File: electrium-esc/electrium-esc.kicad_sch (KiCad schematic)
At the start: 31 parts, among them J2 USB_MICRO, J4 SERVO, J5 Conn_01x04_Male

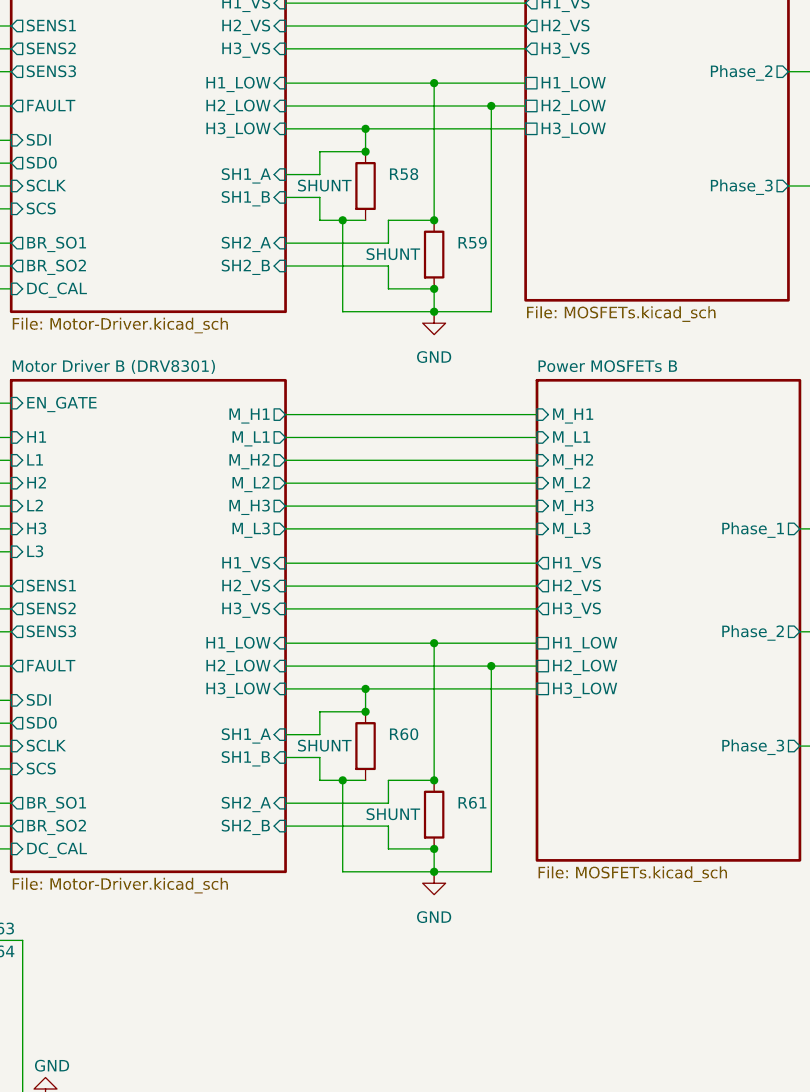
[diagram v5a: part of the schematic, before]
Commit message: Add Shunt resistors and fixed DRC errors
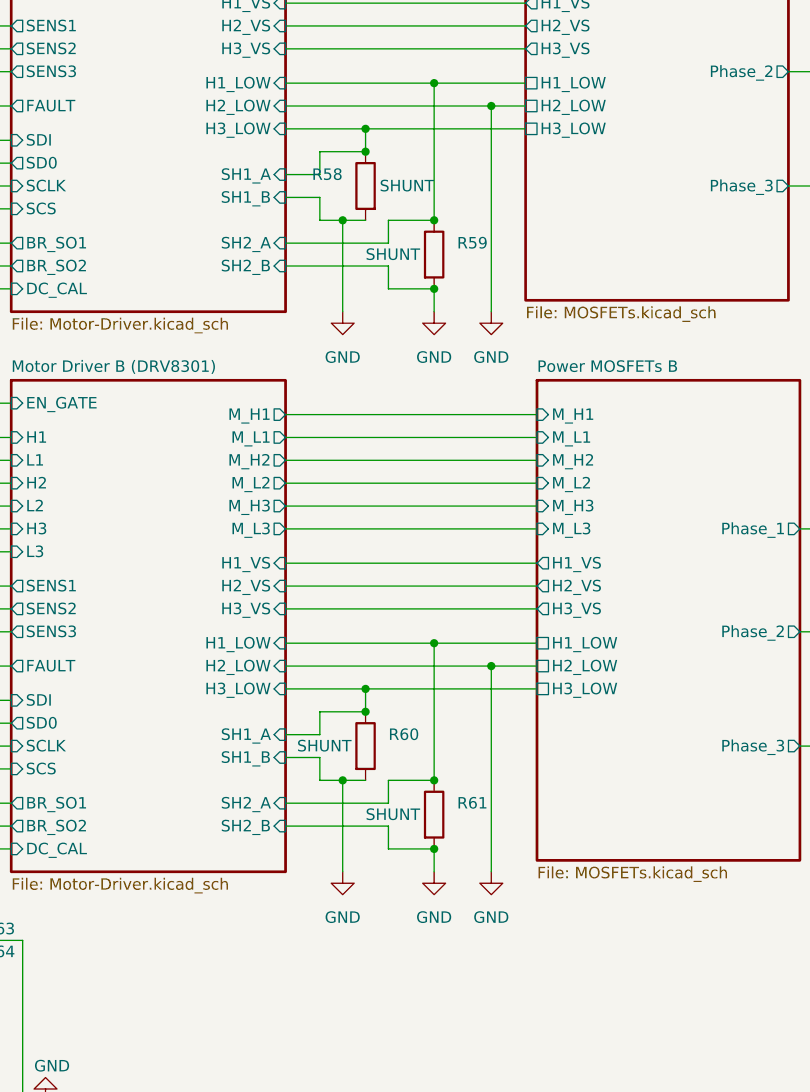
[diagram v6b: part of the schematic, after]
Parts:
- D5: footprint Diode_SMD:D_0201_0603Metric -> Diode_SMD:D_0603_1608Metric
- D6: footprint Diode_SMD:D_0201_0603Metric -> Diode_SMD:D_0402_1005Metric
- R58, R59, R60, R61: footprint Resistor_SMD:R_Shunt_Ohmite_LVK12 -> Resistor_SMD:R_2512_6332Metric
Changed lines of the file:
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@@
   (junction (at 207.01 137.16) (diameter 0) (color 0 0 0 0)
   )
-  (junction (at 214.63 92.71) (diameter 0) (color 0 0 0 0)
-  )
   (junction (at 204.47 82.55) (diameter 0) (color 0 0 0 0)
   )
@@
   (junction (at 207.01 74.93) (diameter 0) (color 0 0 0 0)
   )
-  (junction (at 214.63 154.94) (diameter 0) (color 0 0 0 0)
-  )
   (junction (at 214.63 67.31) (diameter 0) (color 0 0 0 0)
   )
@@
   (junction (at 66.04 43.18) (diameter 0) (color 0 0 0 0)
   )
-  (no_connect (at 53.34 66.04))
   (no_connect (at 85.09 83.82))
   (no_connect (at 85.09 81.28))
+  (no_connect (at 53.34 66.04))
   (no_connect (at 53.34 58.42))
   (wire (pts (xy 152.4 116.84) (xy 167.64 116.84))
@@
     (stroke (width 0) (type default) (color 0 0 0 0))
   )
-  (wire (pts (xy 204.47 92.71) (xy 214.63 92.71))
-    (stroke (width 0) (type default) (color 0 0 0 0))
-  )
   (wire (pts (xy 254 54.61) (xy 262.89 54.61))
     (stroke (width 0) (type default) (color 0 0 0 0))
@@
     (stroke (width 0) (type default) (color 0 0 0 0))
   )
-  (wire (pts (xy 220.98 92.71) (xy 214.63 92.71))
-    (stroke (width 0) (type default) (color 0 0 0 0))
-  )
   (wire (pts (xy 198.12 123.19) (xy 226.06 123.19))
     (stroke (width 0) (type default) (color 0 0 0 0))
@@
     (stroke (width 0) (type default) (color 0 0 0 0))
   )
-  (wire (pts (xy 204.47 154.94) (xy 214.63 154.94))
-    (stroke (width 0) (type default) (color 0 0 0 0))
-  )
   (wire (pts (xy 152.4 114.3) (xy 167.64 114.3))
     (stroke (width 0) (type default) (color 0 0 0 0))
@@
   )
   (wire (pts (xy 152.4 165.1) (xy 157.48 165.1))
-    (stroke (width 0) (type default) (color 0 0 0 0))
-  )
-  (wire (pts (xy 220.98 154.94) (xy 214.63 154.94))
     (stroke (width 0) (type default) (color 0 0 0 0))
   )
@@
     (pin "1")
   )
-  (symbol (lib_id "Device:R") (at 207.01 78.74 0) (unit 1)
-    (in_bom yes) (on_board yes)
-    (property "Reference" "R58" (id 0) (at 209.55 77.4699 0)
-      (effects (font (size 1.27 1.27)) (justify left))
-    )
-    (property "Value" "SHUNT" (id 1) (at 199.39 78.74 0)
-      (effects (font (size 1.27 1.27)) (justify left))
-    )
-    (property "Footprint" "Resistor_SMD:R_Shunt_Ohmite_LVK12" (id 2) (at 205.232 78.74 90)
+  (symbol (lib_id "Device:R") (at 207.01 78.74 0) (mirror y) (unit 1)
+    (in_bom yes) (on_board yes)
+    (property "Reference" "R58" (id 0) (at 204.47 77.4699 0)
+      (effects (font (size 1.27 1.27)) (justify left))
+    )
+    (property "Value" "SHUNT" (id 1) (at 214.63 78.74 0)
+      (effects (font (size 1.27 1.27)) (justify left))
+    )
+    (property "Footprint" "Resistor_SMD:R_2512_6332Metric" (id 2) (at 208.788 78.74 90)
       (effects (font (size 1.27 1.27)) hide)
     )
@@
       (effects (font (size 1.27 1.27)) (justify right))
     )
-    (property "Footprint" "Diode_SMD:D_0201_0603Metric" (id 2) (at 39.37 182.88 0)
+    (property "Footprint" "Diode_SMD:D_0603_1608Metric" (id 2) (at 39.37 182.88 0)
       (effects (font (size 1.27 1.27)) hide)
     )
@@
     (pin "2")
   )
+  (symbol (lib_id "power:GND") (at 220.98 154.94 0) (unit 1)
+    (in_bom yes) (on_board yes) (fields_autoplaced)
+    (property "Reference" "#PWR0103" (id 0) (at 220.98 161.29 0)
+      (effects (font (size 1.27 1.27)) hide)
+    )
+    (property "Value" "GND" (id 1) (at 220.98 160.02 0))
+    (property "Footprint" "" (id 2) (at 220.98 154.94 0)
+      (effects (font (size 1.27 1.27)) hide)
+    )
+    (property "Datasheet" "" (id 3) (at 220.98 154.94 0)
+      (effects (font (size 1.27 1.27)) hide)
+    )
+    (pin "1")
+  )
   (symbol (lib_id "power:GND") (at 34.29 38.1 270) (unit 1)
     (in_bom yes) (on_board yes) (fields_autoplaced)
@@
       (effects (font (size 1.27 1.27)) (justify left))
     )
-    (property "Footprint" "Resistor_SMD:R_Shunt_Ohmite_LVK12" (id 2) (at 205.232 140.97 90)
+    (property "Footprint" "Resistor_SMD:R_2512_6332Metric" (id 2) (at 205.232 140.97 90)
       (effects (font (size 1.27 1.27)) hide)
     )
@@
       (effects (font (size 1.27 1.27)) (justify right))
     )
-    (property "Footprint" "Diode_SMD:D_0201_0603Metric" (id 2) (at 118.11 182.88 0)
+    (property "Footprint" "Diode_SMD:D_0402_1005Metric" (id 2) (at 118.11 182.88 0)
       (effects (font (size 1.27 1.27)) hide)
     )
@@
     (pin "1")
     (pin "2")
+  )
+  (symbol (lib_id "power:GND") (at 204.47 154.94 0) (unit 1)
+    (in_bom yes) (on_board yes) (fields_autoplaced)
+    (property "Reference" "#PWR0102" (id 0) (at 204.47 161.29 0)
+      (effects (font (size 1.27 1.27)) hide)
+    )
+    (property "Value" "GND" (id 1) (at 204.47 160.02 0))
+    (property "Footprint" "" (id 2) (at 204.47 154.94 0)
+      (effects (font (size 1.27 1.27)) hide)
+    )
+    (property "Datasheet" "" (id 3) (at 204.47 154.94 0)
+      (effects (font (size 1.27 1.27)) hide)
+    )
+    (pin "1")
   )
   (symbol (lib_id "power:GND") (at 257.81 25.4 0) (unit 1)
@@
       (effects (font (size 1.27 1.27)) (justify left))
     )
-    (property "Footprint" "Resistor_SMD:R_Shunt_Ohmite_LVK12" (id 2) (at 212.852 148.59 90)
+    (property "Footprint" "Resistor_SMD:R_2512_6332Metric" (id 2) (at 212.852 148.59 90)
       (effects (font (size 1.27 1.27)) hide)
     )
@@
     (pin "3")
     (pin "4")
+  )
+  (symbol (lib_id "power:GND") (at 204.47 92.71 0) (unit 1)
+    (in_bom yes) (on_board yes) (fields_autoplaced)
+    (property "Reference" "#PWR0105" (id 0) (at 204.47 99.06 0)
+      (effects (font (size 1.27 1.27)) hide)
+    )
+    (property "Value" "GND" (id 1) (at 204.47 97.79 0))
+    (property "Footprint" "" (id 2) (at 204.47 92.71 0)
+      (effects (font (size 1.27 1.27)) hide)
+    )
+    (property "Datasheet" "" (id 3) (at 204.47 92.71 0)
+      (effects (font (size 1.27 1.27)) hide)
+    )
+    (pin "1")
   )
   (symbol (lib_id "Connector:Conn_01x03_Male") (at 58.42 163.83 0) (unit 1)
@@
       (effects (font (size 1.27 1.27)) (justify left))
     )
-    (property "Footprint" "Resistor_SMD:R_Shunt_Ohmite_LVK12" (id 2) (at 212.852 86.36 90)
+    (property "Footprint" "Resistor_SMD:R_2512_6332Metric" (id 2) (at 212.852 86.36 90)
       (effects (font (size 1.27 1.27)) hide)
     )
@@
     (pin "1")
     (pin "2")
+  )
+  (symbol (lib_id "power:GND") (at 220.98 92.71 0) (unit 1)
+    (in_bom yes) (on_board yes) (fields_autoplaced)
+    (property "Reference" "#PWR0104" (id 0) (at 220.98 99.06 0)
+      (effects (font (size 1.27 1.27)) hide)
+    )
+    (property "Value" "GND" (id 1) (at 220.98 97.79 0))
+    (property "Footprint" "" (id 2) (at 220.98 92.71 0)
+      (effects (font (size 1.27 1.27)) hide)
+    )
+    (property "Datasheet" "" (id 3) (at 220.98 92.71 0)
+      (effects (font (size 1.27 1.27)) hide)
+    )
+    (pin "1")
   )
   (sheet (at 167.64 38.1) (size 30.48 54.61) (fields_autoplaced)
@@
       (reference "#PWR0101") (unit 1) (value "+3.3V") (footprint "")
     )
+    (path "/8683d831-edf7-449a-ac58-aa35d1700e31"
+      (reference "#PWR0102") (unit 1) (value "GND") (footprint "")
+    )
+    (path "/51499dc7-aa8b-43b4-ae16-4f727d320a69"
+      (reference "#PWR0103") (unit 1) (value "GND") (footprint "")
+    )
+    (path "/ff7a2520-db6a-45d2-a3d1-82acb22ddad7"
+      (reference "#PWR0104") (unit 1) (value "GND") (footprint "")
+    )
+    (path "/93600ca6-ce1a-42ff-90f2-aeacd81c8b54"
+      (reference "#PWR0105") (unit 1) (value "GND") (footprint "")
+    )
     (path "/95515899-f309-4706-b478-ef0c1d74de3d/6e926fcb-bc57-4a6a-ac9a-7920661fd921"
       (reference "C1") (unit 1) (value "4.7u") (footprint "Capacitor_SMD:C_0603_1608Metric")
@@
     )
     (path "/5098eb75-ab3f-49e8-b692-4372bb393d18"
-      (reference "D5") (unit 1) (value "LED") (footprint "Diode_SMD:D_0201_0603Metric")
+      (reference "D5") (unit 1) (value "LED") (footprint "Diode_SMD:D_0603_1608Metric")
     )
     (path "/7f26220b-cbe5-4e56-a50a-18cee9866600"
-      (reference "D6") (unit 1) (value "LED") (footprint "Diode_SMD:D_0201_0603Metric")
+      (reference "D6") (unit 1) (value "LED") (footprint "Diode_SMD:D_0402_1005Metric")
     )
     (path "/95515899-f309-4706-b478-ef0c1d74de3d/ab272a38-ae91-43cc-8c37-b105b22f7c71"
@@
     )
     (path "/0d76d2ab-30c8-46af-9b66-78611601234d"
-      (reference "R58") (unit 1) (value "SHUNT") (footprint "Resistor_SMD:R_Shunt_Ohmite_LVK12")
+      (reference "R58") (unit 1) (value "SHUNT") (footprint "Resistor_SMD:R_2512_6332Metric")
     )
     (path "/dda41dfd-a052-464e-bcc4-258ade89f20e"
-      (reference "R59") (unit 1) (value "SHUNT") (footprint "Resistor_SMD:R_Shunt_Ohmite_LVK12")
+      (reference "R59") (unit 1) (value "SHUNT") (footprint "Resistor_SMD:R_2512_6332Metric")
     )
     (path "/6cdbf01c-e083-42ce-985b-014d3c81c0db"
-      (reference "R60") (unit 1) (value "SHUNT") (footprint "Resistor_SMD:R_Shunt_Ohmite_LVK12")
+      (reference "R60") (unit 1) (value "SHUNT") (footprint "Resistor_SMD:R_2512_6332Metric")
     )
     (path "/8ef27b21-7861-4134-9919-20b00054447c"
-      (reference "R61") (unit 1) (value "SHUNT") (footprint "Resistor_SMD:R_Shunt_Ohmite_LVK12")
+      (reference "R61") (unit 1) (value "SHUNT") (footprint "Resistor_SMD:R_2512_6332Metric")
     )
     (path "/f87270f8-1404-4b4c-885f-44615cc1b15b"

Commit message: Fix warnings
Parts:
- D5: footprint Diode_SMD:D_0603_1608Metric -> Diode_SMD:D_0402_1005Metric
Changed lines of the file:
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@@
       (effects (font (size 1.27 1.27)) (justify right))
     )
-    (property "Footprint" "Diode_SMD:D_0603_1608Metric" (id 2) (at 39.37 182.88 0)
+    (property "Footprint" "Diode_SMD:D_0402_1005Metric" (id 2) (at 39.37 182.88 0)
       (effects (font (size 1.27 1.27)) hide)
     )
@@
     )
     (path "/5098eb75-ab3f-49e8-b692-4372bb393d18"
-      (reference "D5") (unit 1) (value "LED") (footprint "Diode_SMD:D_0603_1608Metric")
+      (reference "D5") (unit 1) (value "LED") (footprint "Diode_SMD:D_0402_1005Metric")
     )
     (path "/7f26220b-cbe5-4e56-a50a-18cee9866600"

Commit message: Add Gerber and final files
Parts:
- D3, D4: footprint Diode_SMD:D_SOD-123 -> Diode_SMD:D_SMA
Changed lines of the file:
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@@
     (property "Reference" "D3" (id 0) (at 41.91 26.67 0))
     (property "Value" "1N5819" (id 1) (at 41.91 31.75 0))
-    (property "Footprint" "Diode_SMD:D_SOD-123" (id 2) (at 45.72 24.765 0)
+    (property "Footprint" "Diode_SMD:D_SMA" (id 2) (at 45.72 24.765 0)
       (effects (font (size 1.27 1.27)) hide)
     )
@@
     (property "Reference" "D4" (id 0) (at 64.77 26.67 0))
     (property "Value" "1N5819" (id 1) (at 64.77 31.75 0))
-    (property "Footprint" "Diode_SMD:D_SOD-123" (id 2) (at 68.58 24.765 0)
+    (property "Footprint" "Diode_SMD:D_SMA" (id 2) (at 68.58 24.765 0)
       (effects (font (size 1.27 1.27)) hide)
     )
@@
     )
     (path "/4dcd2554-0c0c-4fca-b220-d2fb156d9cf9/2194da5e-abcb-490c-ad12-09330a88057c"
-      (reference "D1") (unit 1) (value "1N5819") (footprint "Diode_SMD:D_SOD-123")
+      (reference "D1") (unit 1) (value "1N5819") (footprint "Diode_SMD:D_SMA")
     )
     (path "/8c1d7bfe-a7ad-4b08-9e6d-dd7b239bc0ed/2194da5e-abcb-490c-ad12-09330a88057c"
-      (reference "D2") (unit 1) (value "1N5819") (footprint "Diode_SMD:D_SOD-123")
+      (reference "D2") (unit 1) (value "1N5819") (footprint "Diode_SMD:D_SMA")
     )
     (path "/3c103bef-0efb-4142-b313-3083a43ce99d"
-      (reference "D3") (unit 1) (value "1N5819") (footprint "Diode_SMD:D_SOD-123")
+      (reference "D3") (unit 1) (value "1N5819") (footprint "Diode_SMD:D_SMA")
     )
     (path "/7c2a1523-547e-41f9-846d-b97ecea82980"
-      (reference "D4") (unit 1) (value "1N5819") (footprint "Diode_SMD:D_SOD-123")
+      (reference "D4") (unit 1) (value "1N5819") (footprint "Diode_SMD:D_SMA")
     )
     (path "/5098eb75-ab3f-49e8-b692-4372bb393d18"
